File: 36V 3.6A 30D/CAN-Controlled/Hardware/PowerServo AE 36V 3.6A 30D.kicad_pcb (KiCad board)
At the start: 4 copper layers, 30 x 35.7 mm, 27 parts, among them J1 Control_In, J2 MOT_A, J3 Prog_IN, J4 Power_In, J6 Control_In, J7 MOT_B, U1 LMZM23601V5, U2 TLV76733DRVx, U3 DRV8871DDA, U4 MA730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

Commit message: Fixed U2 / C7 Orientation
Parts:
- moved C5 2.08 mm to (97.4, 84.3), turned to -90 degrees
- moved C6 1.44 mm to (93.7, 84.3), turned to 90 degrees
- moved C7 0.89 mm to (92.2, 82.2), turned to 90 degrees
- moved U2 0.79 mm to (95.6, 84.8), turned to 0 degrees
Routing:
- net GND: vias 119 -> 148
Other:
- board text added: "SMART SERVO by Alex C V 0.7"
- board text removed: "SMART SERVO by Alex C V 0.6"

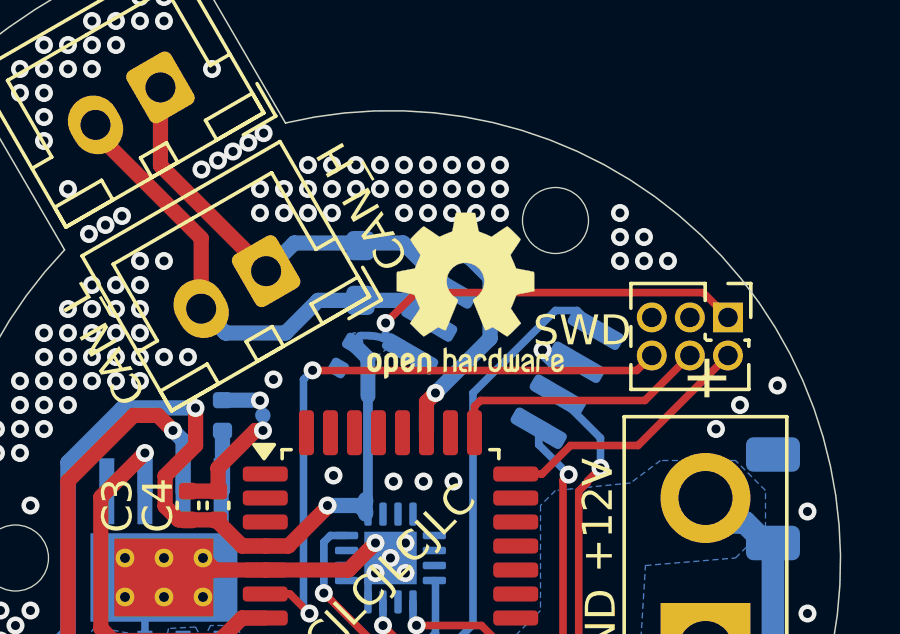
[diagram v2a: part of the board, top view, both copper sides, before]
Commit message: Bumped to V0.7
Following Reddit Review:
- Added C10 as NRST Cap
- Added R3 as Boot0/SWCLK Pull-Down
- Added Solder Jumper for CAN Termination
-- Downscaled R2
- Fixed some of the odd orientations of components
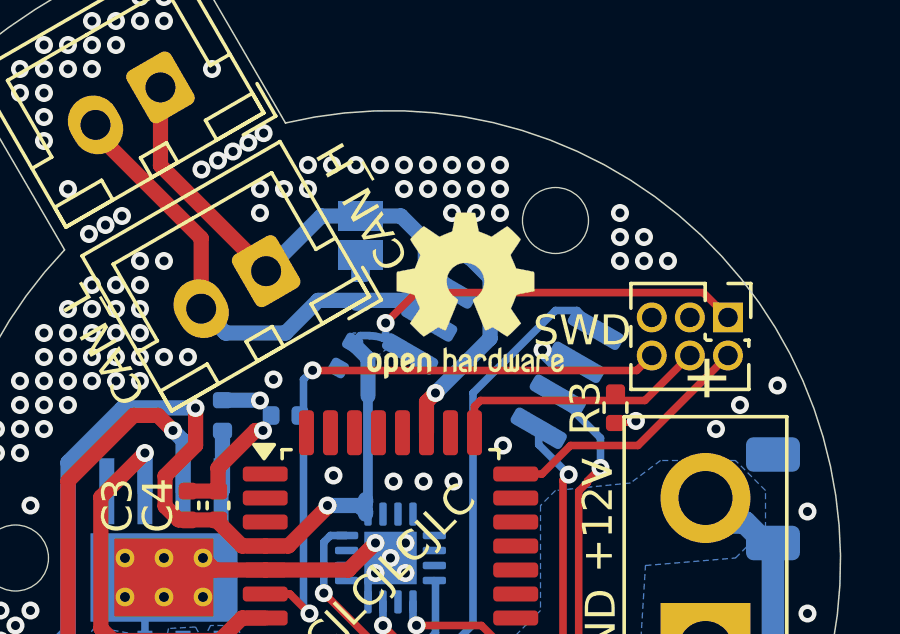
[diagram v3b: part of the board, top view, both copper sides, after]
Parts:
- added C10: 100nF, Capacitor_SMD:C_0402_1005Metric, B.Cu at (90.0, 68.0)
- added JP1: Jumper_2_Open, Jumper:SolderJumper-2_P1.3mm_Open_Pad1.0x1.5mm, B.Cu at (92.5, 62.0)
- added R3: 10k, Resistor_SMD:R_0402_1005Metric, F.Cu at (101.0, 67.7)
- R2: footprint Resistor_SMD:R_0603_1608Metric_Pad0.98x0.95mm_HandSolder -> Capacitor_SMD:C_0402_1005Metric
- moved R2 0.50 mm to (92.5, 63.8)
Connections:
- R2 pad 1: CAN_H -> Net-(JP1-A)
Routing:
- net CAN_H: track 14.7 -> 15.9 mm
- net GND: track 24.9 -> 25.4 mm, vias 148 -> 142

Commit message: I forgor
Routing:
- net GND: track 25.4 -> 24.5 mm, vias 142 -> 143
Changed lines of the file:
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@@
 	(gr_rect
 		(start 75.25 51.75)
-		(end 111.75 88.25)
+		(end 112.25 88.25)
 		(stroke
 			(width 0.1)
@@
 	)
 	(segment
-		(start 89 68.5)
-		(end 87.75 69.75)
-		(width 0.508)
-		(layer "F.Cu")
-		(net 1)
-	)
-	(segment
-		(start 87.75 69.75)
-		(end 87.75 70.52)
-		(width 0.508)
-		(layer "F.Cu")
-		(net 1)
-	)
-	(segment
 		(start 101.613288 68.25)
 		(end 101.681644 68.181644)
@@
 	)
 	(segment
-		(start 89.325 73.15)
-		(end 92.1 73.15)
-		(width 0.508)
-		(layer "F.Cu")
-		(net 1)
-	)
-	(segment
-		(start 92.1 73.15)
+		(start 91.75 72.25)
 		(end 93 72.25)
 		(width 0.508)
@@
 	)
 	(segment
-		(start 89.25 68.5)
-		(end 89 68.5)
+		(start 87.75 69.75)
+		(end 87.75 70.52)
 		(width 0.508)
 		(layer "F.Cu")
@@
 		(start 87.65 73.15)
 		(end 87.25 72.75)
+		(width 0.508)
+		(layer "F.Cu")
+		(net 1)
+	)
+	(segment
+		(start 88.875 68.625)
+		(end 87.75 69.75)
+		(width 0.508)
+		(layer "F.Cu")
+		(net 1)
+	)
+	(segment
+		(start 89.325 73.15)
+		(end 90.85 73.15)
 		(width 0.508)
 		(layer "F.Cu")
@@
 		(net 1)
 	)
+	(segment
+		(start 90.85 73.15)
+		(end 91.75 72.25)
+		(width 0.508)
+		(layer "F.Cu")
+		(net 1)
+	)
 	(via
 		(at 101.15 62.05)
@@
 	)
 	(via
-		(at 89.25 68.5)
+		(at 88.875 68.625)
 		(size 0.6)
 		(drill 0.3)
@@
 	)
 	(via
-		(at 89.149998 67.500002)
+		(at 88.75 67.490003)
 		(size 0.6)
 		(drill 0.3)
@@
 	)
 	(via
-		(at 89.6 66.8)
+		(at 89.75 66.5)
 		(size 0.6)
 		(drill 0.3)
@@
 	)
 	(via
+		(at 91.25 65.5)
+		(size 0.6)
+		(drill 0.3)
+		(layers "F.Cu" "B.Cu")
+		(free yes)
+		(net 1)
+	)
+	(via
 		(at 90.75 86.05)
 		(size 0.6)
@@
 		(layers "F.Cu" "B.Cu")
 		(free yes)
-		(net 1)
-	)
-	(segment
-		(start 87.9 67.490003)
-		(end 89.139999 67.490003)
-		(width 0.508)
-		(layer "B.Cu")
 		(net 1)
 	)
@@
 	)
 	(segment
+		(start 87.9 67.490003)
+		(end 88.75 67.490003)
+		(width 0.508)
+		(layer "B.Cu")
+		(net 1)
+	)
+	(segment
 		(start 103.595 79.05)
 		(end 103.425001 79.219999)
@@
 	)
 	(segment
-		(start 86.440001 71.48)
-		(end 85.986 71.025999)
-		(width 0.508)
-		(layer "F.Cu")
-		(net 2)
-	)
-	(segment
 		(start 103.922997 63.902996)
 		(end 94.351506 63.902996)
@@
 	)
 	(segment
+		(start 85.986 71.025999)
+		(end 86.440001 71.48)
+		(width 0.508)
+		(layer "F.Cu")
+		(net 2)
+	)
+	(segment
 		(start 87.75 71.48)
 		(end 87.75 71.547294)
+		(width 0.508)
+		(layer "F.Cu")
+		(net 2)
+	)
+	(segment
+		(start 87.004 68.996)
+		(end 85.986 70.014)
 		(width 0.508)
 		(layer "F.Cu")
@@
 	)
 	(segment
-		(start 86.75 71.48)
-		(end 86.440001 71.48)
-		(width 0.508)
-		(layer "F.Cu")
-		(net 2)
-	)
-	(segment
-		(start 87.004 67.754)
-		(end 87 67.75)
-		(width 0.508)
-		(layer "F.Cu")
-		(net 2)
-	)
-	(segment
 		(start 91.4 71.047294)
 		(end 90.097294 72.35)
@@
 	)
 	(segment
-		(start 87.004 68.996)
-		(end 87.004 67.754)
-		(width 0.508)
-		(layer "F.Cu")
-		(net 2)
-	)
-	(segment
-		(start 85.986 70.014)
-		(end 87.004 68.996)
-		(width 0.508)
-		(layer "F.Cu")
-		(net 2)
-	)
-	(segment
 		(start 90.097294 72.35)
 		(end 89.325 72.35)
@@
 	)
 	(segment
-		(start 85.986 71.025999)
-		(end 85.986 70.014)
+		(start 85.986 70.014)
+		(end 85.986 71.025999)
+		(width 0.508)
+		(layer "F.Cu")
+		(net 2)
+	)
+	(segment
+		(start 87.036948 68.220629)
+		(end 87.004 68.253577)
 		(width 0.508)
 		(layer "F.Cu")
@@
 	)
 	(segment
+		(start 86.440001 71.48)
+		(end 86.75 71.48)
+		(width 0.508)
+		(layer "F.Cu")
+		(net 2)
+	)
+	(segment
 		(start 91.4 71)
 		(end 91.4 71.047294)
@@
 	)
 	(segment
+		(start 87.004 68.253577)
+		(end 87.004 68.996)
+		(width 0.508)
+		(layer "F.Cu")
+		(net 2)
+	)
+	(segment
 		(start 88.552706 72.35)
 		(end 89.325 72.35)
@@
 	)
 	(via
-		(at 87 67.75)
+		(at 87.036948 68.220629)
 		(size 0.6)
 		(drill 0.3)
@@
 		(drill 0.3)
 		(layers "F.Cu" "B.Cu")
+		(net 2)
+	)
+	(segment
+		(start 84.566 67.746)
+		(end 82.75 69.562)
+		(width 0.508)
+		(layer "B.Cu")
 		(net 2)
 	)
@@
 		(start 92.671 70.879)
 		(end 92.671 70.8)
-		(width 0.508)
-		(layer "B.Cu")
-		(net 2)
-	)
-	(segment
-		(start 86.996 67.746)
-		(end 84.566 67.746)
-		(width 0.508)
-		(layer "B.Cu")
-		(net 2)
-	)
-	(segment
-		(start 84.566 67.746)
-		(end 82.75 69.562)
 		(width 0.508)
 		(layer "B.Cu")
@@
 	)
 	(segment
-		(start 81.8 76.2)
-		(end 81.8 80.552534)
-		(width 0.508)
-		(layer "B.Cu")
-		(net 2)
-	)
-	(segment
-		(start 89.530002 84.780002)
-		(end 93.657501 84.780002)
-		(width 0.508)
-		(layer "B.Cu")
-		(net 2)
-	)
-	(segment
 		(start 92.24 65.584308)
 		(end 92.75 66.094308)
@@
 	)
 	(segment
-		(start 84.247466 83)
-		(end 87.75 83)
-		(width 0.508)
-		(layer "B.Cu")
-		(net 2)
-	)
-	(segment
-		(start 81.8 80.552534)
-		(end 84.247466 83)
-		(width 0.508)
-		(layer "B.Cu")
-		(net 2)
-	)
-	(segment
 		(start 92.24 65.584308)
 		(end 92.48799 65.336318)
@@
 	)
 	(segment
+		(start 87.75 83)
+		(end 89.530002 84.780002)
+		(width 0.508)
+		(layer "B.Cu")
+		(net 2)
+	)
+	(segment
+		(start 84.247466 83)
+		(end 87.75 83)
+		(width 0.508)
+		(layer "B.Cu")
+		(net 2)
+	)
+	(segment
 		(start 92.55 71)
 		(end 92.55 71.0875)
@@
 	)
 	(segment
-		(start 87 67.75)
-		(end 86.996 67.746)
-		(width 0.508)
-		(layer "B.Cu")
-		(net 2)
-	)
-	(segment
 		(start 91.4 71)
 		(end 92.55 71)
@@
 	)
 	(segment
-		(start 87.75 83)
-		(end 89.530002 84.780002)
+		(start 89.530002 84.780002)
+		(end 93.657501 84.780002)
+		(width 0.508)
+		(layer "B.Cu")
+		(net 2)
+	)
+	(segment
+		(start 82.75 69.562)
+		(end 82.75 75.25)
+		(width 0.508)
+		(layer "B.Cu")
+		(net 2)
+	)
+	(segment
+		(start 86.562319 67.746)
+		(end 84.566 67.746)
+		(width 0.508)
+		(layer "B.Cu")
+		(net 2)
+	)
+	(segment
+		(start 87.036948 68.220629)
+		(end 86.562319 67.746)
 		(width 0.508)
 		(layer "B.Cu")
@@
 	)
 	(segment
+		(start 81.8 76.2)
+		(end 81.8 80.552534)
+		(width 0.508)
+		(layer "B.Cu")
+		(net 2)
+	)
+	(segment
+		(start 81.8 80.552534)
+		(end 84.247466 83)
+		(width 0.508)
+		(layer "B.Cu")
+		(net 2)
+	)
+	(segment
 		(start 92.55 71.0875)
 		(end 92.671 71.2085)
@@
 		(width 0.508)
 		(layer "B.Cu")
-		(net 2)
-	)
-	(segment
-		(start 82.75 69.562)
-		(end 82.75 75.25)
-		(width 0.508)
-		(layer "B.Cu")
